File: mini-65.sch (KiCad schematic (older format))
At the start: 173 parts, among them J1 TYPE-C-31-M12_13_EDITED, J2 AVR-ISP-6, SW1 SW_Push, U1 ATmega32U4-AU, U2 WE-TVS-82400102, Y1 Crystal_GND24_Small

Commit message: changed layout of schematic
started the cleanup of the schematic, with nice lines and names above parts
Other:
- note added: "Mechanical Keyswitch Matrix"
- note added: "Microcontroller (atmega32u4)"
- moved on the sheet: C1, C2, C3, C4, C5, C6, C7, C8, D0, D1, D10, D11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

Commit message: Rearranged the schematic
Added lines and text to the different parts of the schematic
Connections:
- wire segments 313 -> 308
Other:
- note added: "Crystal"
- note added: "Decoupling Capacitors"
- note added: "ESD Protection TVS Diode"
- note added: "ICSP Header"
- note added: "Logos"
- note added: "Mounting Holes"
- note added: "Polyfuse"
- note added: "USB Type C"
- moved on the sheet: C1, C2, C3, C4, C5, C6, C7, C8, D0, D1, D10, D11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

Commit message: General schematic information added
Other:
- note added: "Electrical protection"
- note added: "mini eLiXiVy Schematic"
- moved on the sheet: C1, C2, C8, F1, H0, H1, H2, H3, H4, H5, J1, J2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

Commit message: Added different OSHW logo
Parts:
- removed D9: 1N4148W, mini-general-tweaks:D_SOD123_axial-dual, symbol Diode:1N4148W
- removed LO0: mini-eLiXiR-Logo-Mask, mini-Logos:eLiXiVy-Maskv2, symbol mini_random_library:mini-eLiXiR-Logo-Mask
- removed LO1: mini-eLiXiR-Logo-SilkScreen, mini-Logos:eLiXiVy-SilkScreenv2, symbol mini_random_library:mini-eLiXiR-Logo-SilkScreen
- added LO0: mini-eLiXiVy-SilkScreen, mini-Logos:eLiXiVy-SilkScreenv2, symbol mini_random_library:Logo
- added LO1: mini-eLiXiVy-Mask, mini-Logos:eLiXiVy-Maskv2, symbol mini_random_library:Logo
- added LO2: OSHW-Logo, mini-Logos:OSHW-Logo, symbol mini_random_library:Logo
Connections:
- wire segments 308 -> 307

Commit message: moved H3 mounting hole
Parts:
- added D9: 1N4148W, mini-general-tweaks:D_SOD123_axial-dual, symbol Diode:1N4148W
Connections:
- net ROW0: now also D9.1 (K)
- net at MX_9.2 (ROW): now also D9.2 (A)
- net DN: no longer names the net of R3.1, U1.3 (D-)
- net DP: no longer names the net of R2.1, U1.4 (D+)
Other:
- moved on the sheet: C1, C2, C3, C4, C5, C6, C7, C8, D0, D1, D10, D2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

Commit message: Shrunk schematic/matrix to fit on an A4 sheet
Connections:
- net ROW4: no longer D63.1 (K), D64.1 (K), D65.1 (K), D66.1 (K), D67.1 (K), D68.1 (K)
- new net: D63.1 (K), D64.1 (K), D65.1 (K), D66.1 (K), D67.1 (K), D68.1 (K)
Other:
- moved on the sheet: C1, C2, C3, C4, C5, C6, C7, C8, D10, F1, H0, H1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

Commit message: Rearranged the schematic to fit on an A4 sheet
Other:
- note added: "ESD TVS Diode"
- note added: "Electrical Protection"
- note removed: "ESD Protection TVS Diode"
- note removed: "Electrical protection"
- moved on the sheet: C1, C2, C3, C4, C5, C6, C7, C8, D0, D1, D10, D11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

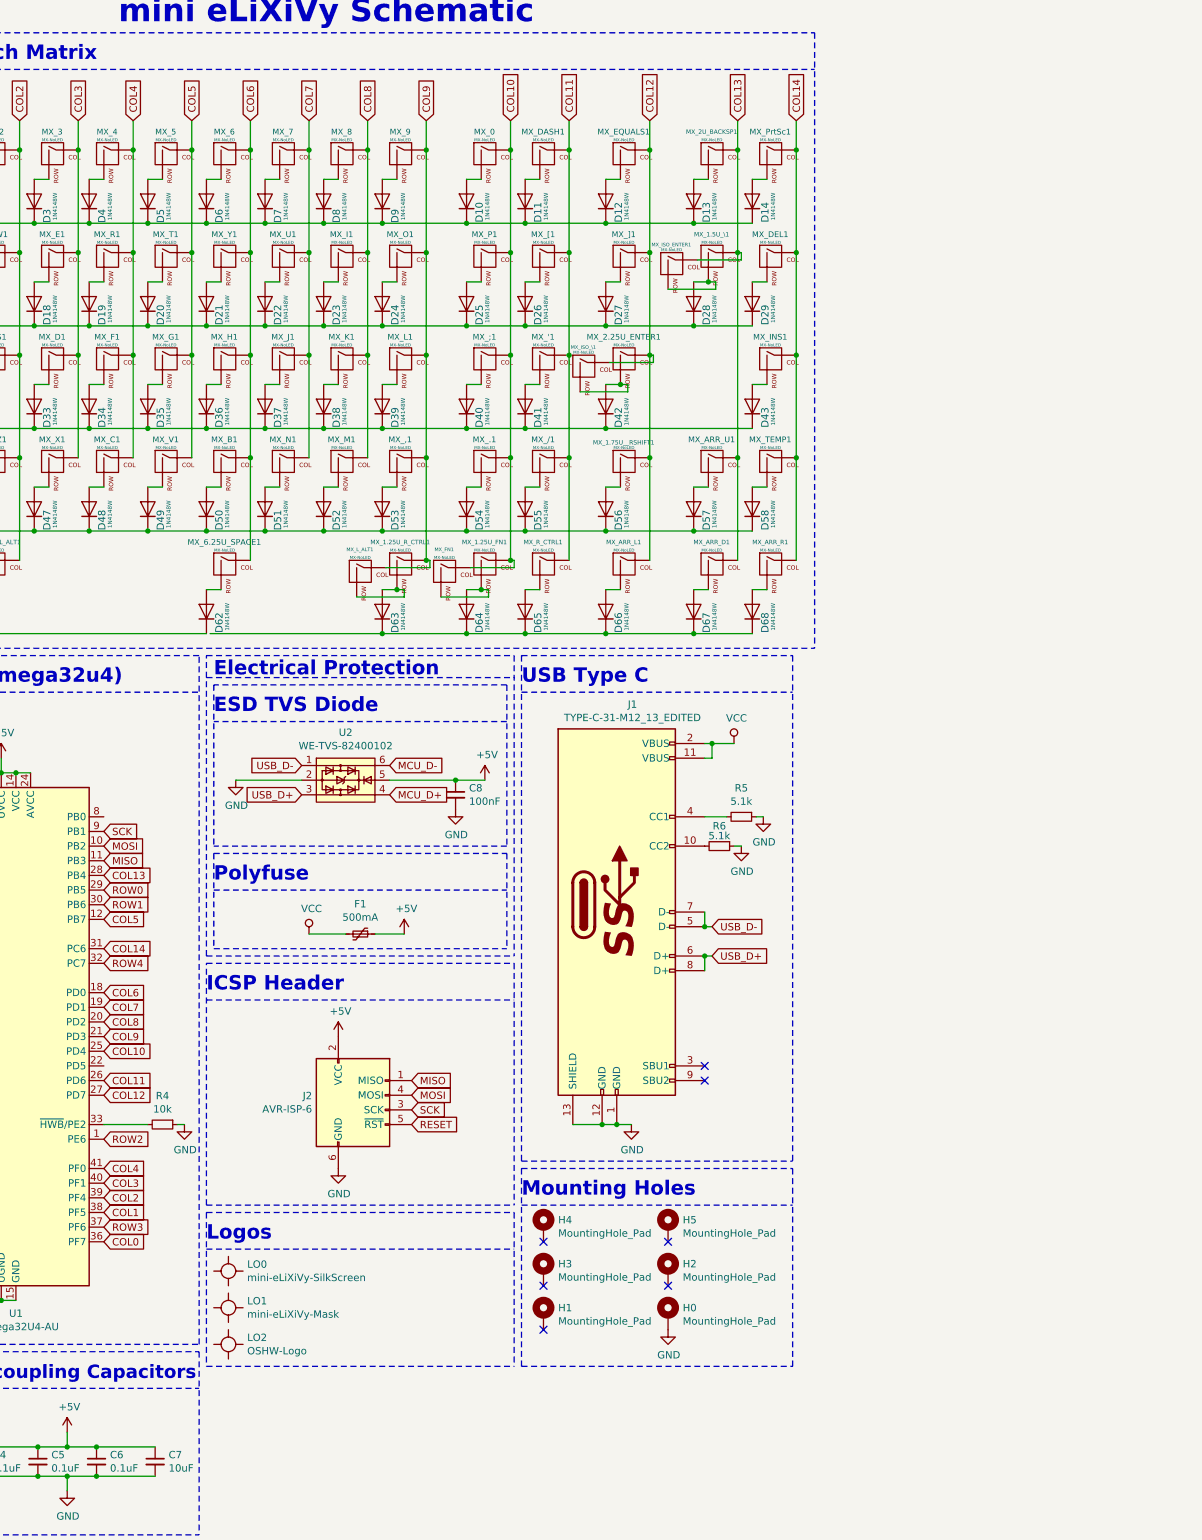
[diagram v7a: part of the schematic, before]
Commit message: Added rotary encoder first steps
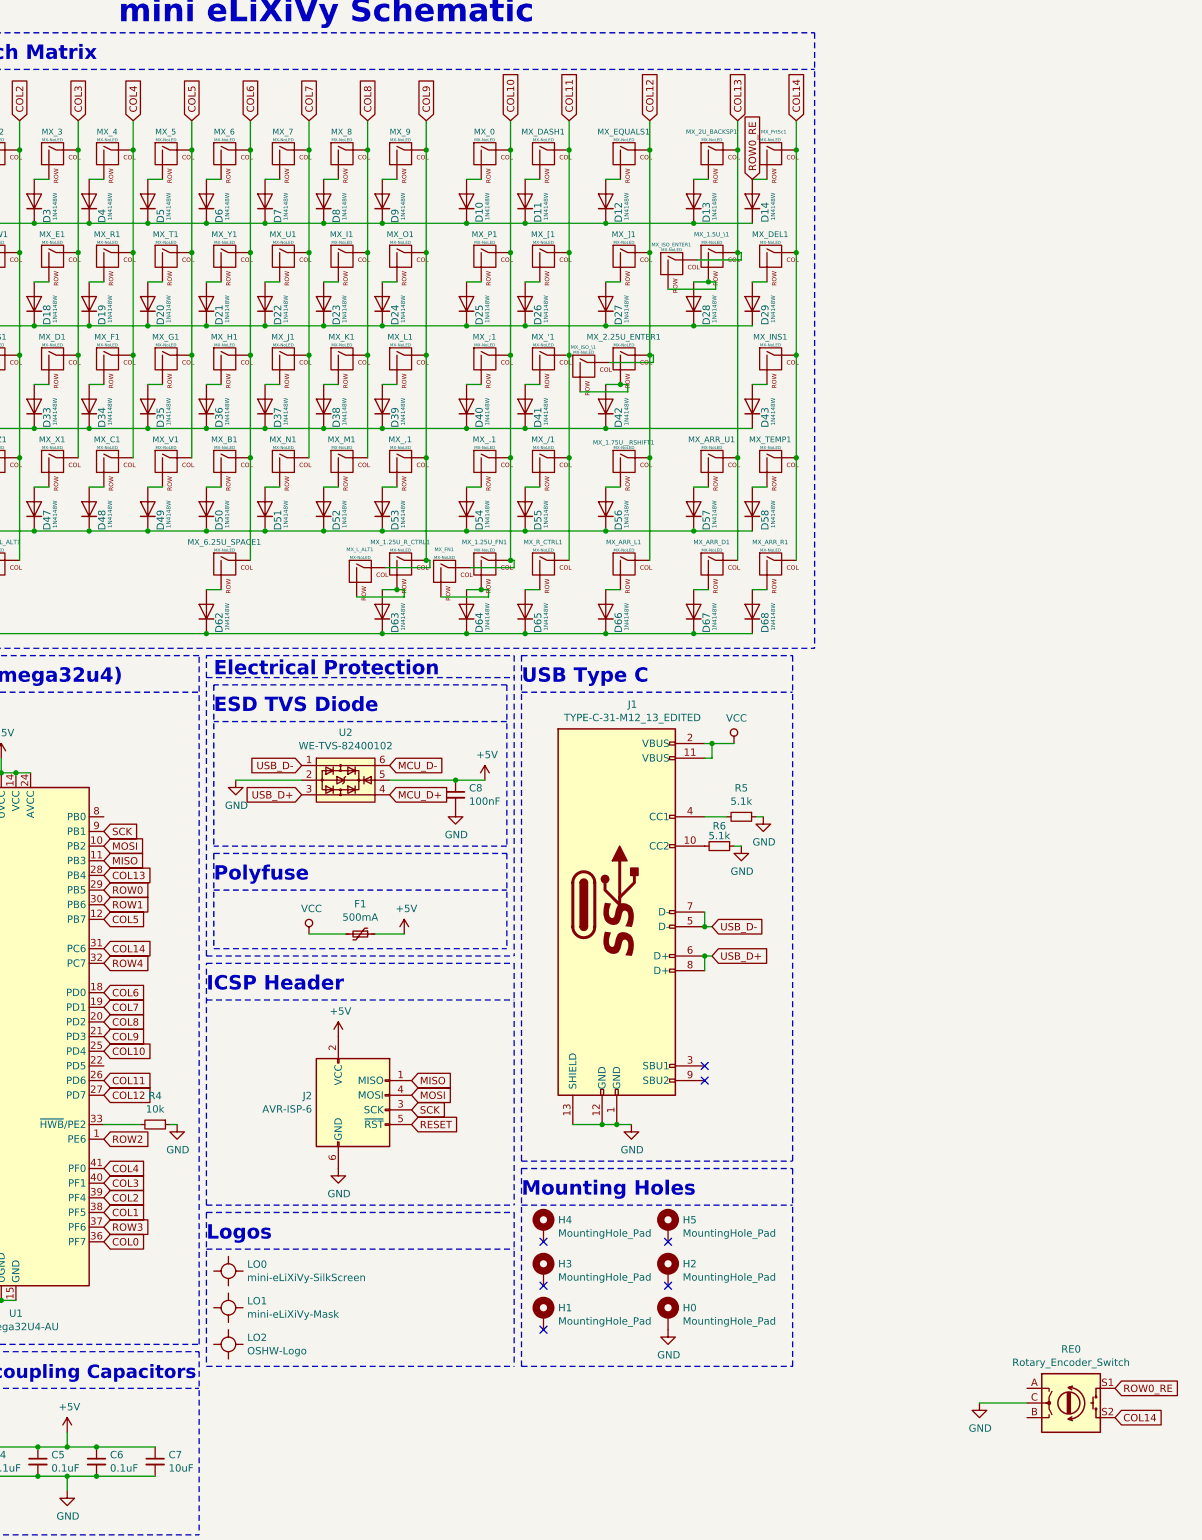
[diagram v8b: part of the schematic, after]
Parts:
- added RE0: Rotary_Encoder_Switch, Rotary_Encoder:RotaryEncoder_Alps_EC11E-Switch_Vertical_H20mm_CircularMountingHoles, symbol Device:Rotary_Encoder_Switch
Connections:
- net COL14: now also RE0.S2
- net GND: now also RE0.C
- net ROW4: now also D63.1 (K), D64.1 (K), D65.1 (K), D66.1 (K), D67.1 (K), D68.1 (K)
- net ROW0_RE: now reaches D14.2 (A), MX_PrtSc1.2 (ROW)
- net ROW0_RE: now also RE0.S1
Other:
- moved on the sheet: R4
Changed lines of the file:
@@
 Wire Wire Line
 	4750 4200 5325 4200
-Connection ~ 6275 4900
 Connection ~ 5725 4900
-Wire Wire Line
-	5725 4900 6275 4900
 Connection ~ 5325 4900
 Connection ~ 4750 4900
@@
 Wire Wire Line
 	3550 4200 3950 4200
-Wire Wire Line
-	6275 4900 6875 4900
 Wire Wire Line
 	6275 4200 6875 4200
@@
 Wire Wire Line
 	1975 4900 3550 4900
-Wire Wire Line
-	3575 4900 4750 4900
 Connection ~ 3850 3700
 Wire Wire Line
 	3850 3700 3850 4400
-Wire Wire Line
-	6875 4900 7275 4900
-Connection ~ 6875 4900
 Wire Wire Line
 	5325 4900 5725 4900
@@
 Wire Wire Line
 	900  2100 1100 2100
-Wire Wire Line
-	7175 3700 7175 4400
-Connection ~ 7175 3700
 Wire Wire Line
 	7175 2300 7175 3700
@@
 Wire Wire Line
 	7175 2300 7200 2300
-Wire Wire Line
-	6575 3700 6575 4400
-Connection ~ 6575 3700
 Wire Wire Line
 	6575 3000 6575 3700
@@
 $EndComp
 $Comp
-L Diode:1N4148W D68
-U 1 1 624EA389
-P 7275 4750
-F 0 "D68" H 7270 4663 50  0000 R CNN
-F 1 "1N4148W" H 7334 4608 28  0000 R CNN
-F 2 "mini-general-tweaks:D_SOD123_axial-dual" H 7275 4575 50  0001 C CNN
-F 3 "https://www.vishay.com/docs/85748/1n4148w.pdf" H 7275 4750 50  0001 C CNN
-	1    7275 4750
-	0    -1   -1   0
-$EndComp
-$Comp
-L Diode:1N4148W D67
-U 1 1 624DD549
-P 6875 4750
-F 0 "D67" H 6870 4663 50  0000 R CNN
-F 1 "1N4148W" H 6934 4608 28  0000 R CNN
-F 2 "mini-general-tweaks:D_SOD123_axial-dual" H 6875 4575 50  0001 C CNN
-F 3 "https://www.vishay.com/docs/85748/1n4148w.pdf" H 6875 4750 50  0001 C CNN
-	1    6875 4750
-	0    -1   -1   0
-$EndComp
-$Comp
-L Diode:1N4148W D66
-U 1 1 624D06BD
-P 6275 4750
-F 0 "D66" H 6270 4663 50  0000 R CNN
-F 1 "1N4148W" H 6334 4608 28  0000 R CNN
-F 2 "mini-general-tweaks:D_SOD123_axial-dual" H 6275 4575 50  0001 C CNN
-F 3 "https://www.vishay.com/docs/85748/1n4148w.pdf" H 6275 4750 50  0001 C CNN
-	1    6275 4750
-	0    -1   -1   0
-$EndComp
-$Comp
 L Diode:1N4148W D65
 U 1 1 624C36E1
@@
 	1250 3900 1250 3950
 Wire Wire Line
-	6975 4600 6875 4600
-$Comp
-L MX_Alps_Hybrid:MX-NoLED MX_ARR_D1
-U 1 1 5F474908
-P 7025 4450
-F 0 "MX_ARR_D1" H 6997 4624 30  0000 C CNN
-F 1 "MX-NoLED" H 6999 4569 20  0000 C CNN
-F 2 "mini-MX-Tweaks:MXOnly-1U-NoLED_tweak" H 6400 4425 60  0001 C CNN
-F 3 "" H 6400 4425 60  0001 C CNN
-	1    7025 4450
-	1    0    0    -1
-$EndComp
-Wire Wire Line
 	6975 2500 6875 2500
 $Comp
@@
 	7375 3900 7275 3900
 Wire Wire Line
-	7375 4600 7275 4600
-Wire Wire Line
 	7375 2500 7275 2500
 $Comp
@@
 $EndComp
 Connection ~ 6975 2500
-$Comp
-L MX_Alps_Hybrid:MX-NoLED MX_ARR_R1
-U 1 1 5F48B682
-P 7425 4450
-F 0 "MX_ARR_R1" H 7397 4624 30  0000 C CNN
-F 1 "MX-NoLED" H 7399 4569 20  0000 C CNN
-F 2 "mini-MX-Tweaks:MXOnly-1U-NoLED_tweak" H 6800 4425 60  0001 C CNN
-F 3 "" H 6800 4425 60  0001 C CNN
-	1    7425 4450
-	1    0    0    -1
-$EndComp
 Wire Wire Line
 	6975 3900 6875 3900
@@
 	6375 2500 6275 2500
 $Comp
-L MX_Alps_Hybrid:MX-NoLED MX_ARR_L1
-U 1 1 5F45D4BC
-P 6425 4450
-F 0 "MX_ARR_L1" H 6397 4624 30  0000 C CNN
-F 1 "MX-NoLED" H 6399 4569 20  0000 C CNN
-F 2 "mini-MX-Tweaks:MXOnly-1U-NoLED_tweak" H 5800 4425 60  0001 C CNN
-F 3 "" H 5800 4425 60  0001 C CNN
-	1    6425 4450
-	1    0    0    -1
-$EndComp
-Wire Wire Line
-	6375 4600 6275 4600
-$Comp
 L MX_Alps_Hybrid:MX-NoLED MX_1.75U_CAPSLOCK1
 U 1 1 5F1A606A
@@
 U 1 1 5F48B6A3
 P 7425 1650
-F 0 "MX_PrtSc1" H 7397 1824 39  0000 C CNN
+F 0 "MX_PrtSc1" H 7421 1824 24  0000 C CNN
 F 1 "MX-NoLED" H 7399 1769 20  0000 C CNN
 F 2 "mini-MX-Tweaks:MXOnly-1U-NoLED_tweak" H 6800 1625 60  0001 C CNN
@@
 L power:GND #PWR0104
 U 1 1 5F16F0E0
-P 3400 8250
-F 0 "#PWR0104" H 3400 8000 50  0001 C CNN
-F 1 "GND" H 3405 8077 50  0000 C CNN
-F 2 "" H 3400 8250 50  0001 C CNN
-F 3 "" H 3400 8250 50  0001 C CNN
-	1    3400 8250
-	1    0    0    -1
-$EndComp
-Wire Wire Line
-	3350 8250 3400 8250
+P 3350 8250
+F 0 "#PWR0104" H 3350 8000 50  0001 C CNN
+F 1 "GND" H 3355 8077 50  0000 C CNN
+F 2 "" H 3350 8250 50  0001 C CNN
+F 3 "" H 3350 8250 50  0001 C CNN
+	1    3350 8250
+	1    0    0    -1
+$EndComp
+Wire Wire Line
+	3300 8250 3350 8250
 $Comp
 L Device:R_Small R4
 U 1 1 5F16CB52
-P 3250 8250
-F 0 "R4" V 3054 8250 50  0000 C CNN
-F 1 "10k" V 3145 8250 50  0000 C CNN
-F 2 "Resistor_SMD:R_0805_2012Metric" H 3250 8250 50  0001 C CNN
-F 3 "~" H 3250 8250 50  0001 C CNN
-	1    3250 8250
+P 3200 8250
+F 0 "R4" V 3004 8250 50  0000 C CNN
+F 1 "10k" V 3095 8250 50  0000 C CNN
+F 2 "Resistor_SMD:R_0805_2012Metric" H 3200 8250 50  0001 C CNN
+F 3 "~" H 3200 8250 50  0001 C CNN
+	1    3200 8250
 	0    1    1    0
 $EndComp
-Wire Wire Line
-	2850 8250 3150 8250
 $Comp
 L power:GND #PWR0106
@@
 Wire Notes Line
 	1900 11050 3500 11050
+Wire Wire Line
+	3550 4900 4750 4900
+Connection ~ 3550 4900
+Text GLabel 7275 1800 1    50   Input ~ 0
+ROW0_RE
+Text GLabel 9750 10050 2    50   Input ~ 0
+ROW0_RE
+Text GLabel 9750 10250 2    50   Input ~ 0
+COL14
+$Comp
+L power:GND #PWR0123
+U 1 1 64F8DD45
+P 8825 10150
+F 0 "#PWR0123" H 8825 9900 50  0001 C CNN
+F 1 "GND" H 8830 9977 50  0000 C CNN
+F 2 "" H 8825 10150 50  0001 C CNN
+F 3 "" H 8825 10150 50  0001 C CNN
+	1    8825 10150
+	1    0    0    -1
+$EndComp
+Wire Wire Line
+	8825 10150 9150 10150
+$Comp
+L Device:Rotary_Encoder_Switch RE0
+U 1 1 64FB0777
+P 9450 10150
+F 0 "RE0" H 9450 10517 50  0000 C CNN
+F 1 "Rotary_Encoder_Switch" H 9450 10426 50  0000 C CNN
+F 2 "Rotary_Encoder:RotaryEncoder_Alps_EC11E-Switch_Vertical_H20mm_CircularMountingHoles" H 9300 10310 50  0001 C CNN
+F 3 "~" H 9450 10410 50  0001 C CNN
+	1    9450 10150
+	1    0    0    -1
+$EndComp
+Wire Wire Line
+	2850 8250 3100 8250
+Connection ~ 6575 3700
+Connection ~ 7175 3700
+Connection ~ 6875 4900
+Wire Wire Line
+	6875 4900 7275 4900
+Wire Wire Line
+	6275 4900 6875 4900
+Wire Wire Line
+	5725 4900 6275 4900
+Connection ~ 6275 4900
+Wire Wire Line
+	6375 4600 6275 4600
+$Comp
+L MX_Alps_Hybrid:MX-NoLED MX_ARR_L1
+U 1 1 5F45D4BC
+P 6425 4450
+F 0 "MX_ARR_L1" H 6397 4624 30  0000 C CNN
+F 1 "MX-NoLED" H 6399 4569 20  0000 C CNN
+F 2 "mini-MX-Tweaks:MXOnly-1U-NoLED_tweak" H 5800 4425 60  0001 C CNN
+F 3 "" H 5800 4425 60  0001 C CNN
+	1    6425 4450
+	1    0    0    -1
+$EndComp
+$Comp
+L MX_Alps_Hybrid:MX-NoLED MX_ARR_R1
+U 1 1 5F48B682
+P 7425 4450
+F 0 "MX_ARR_R1" H 7397 4624 30  0000 C CNN
+F 1 "MX-NoLED" H 7399 4569 20  0000 C CNN
+F 2 "mini-MX-Tweaks:MXOnly-1U-NoLED_tweak" H 6800 4425 60  0001 C CNN
+F 3 "" H 6800 4425 60  0001 C CNN
+	1    7425 4450
+	1    0    0    -1
+$EndComp
+Wire Wire Line
+	7375 4600 7275 4600
+$Comp
+L MX_Alps_Hybrid:MX-NoLED MX_ARR_D1
+U 1 1 5F474908
+P 7025 4450
+F 0 "MX_ARR_D1" H 6997 4624 30  0000 C CNN
+F 1 "MX-NoLED" H 6999 4569 20  0000 C CNN
+F 2 "mini-MX-Tweaks:MXOnly-1U-NoLED_tweak" H 6400 4425 60  0001 C CNN
+F 3 "" H 6400 4425 60  0001 C CNN
+	1    7025 4450
+	1    0    0    -1
+$EndComp
+Wire Wire Line
+	6975 4600 6875 4600
+$Comp
+L Diode:1N4148W D66
+U 1 1 624D06BD
+P 6275 4750
+F 0 "D66" H 6270 4663 50  0000 R CNN
+F 1 "1N4148W" H 6334 4608 28  0000 R CNN
+F 2 "mini-general-tweaks:D_SOD123_axial-dual" H 6275 4575 50  0001 C CNN
+F 3 "https://www.vishay.com/docs/85748/1n4148w.pdf" H 6275 4750 50  0001 C CNN
+	1    6275 4750
+	0    -1   -1   0
+$EndComp
+$Comp
+L Diode:1N4148W D67
+U 1 1 624DD549
+P 6875 4750
+F 0 "D67" H 6870 4663 50  0000 R CNN
+F 1 "1N4148W" H 6934 4608 28  0000 R CNN
+F 2 "mini-general-tweaks:D_SOD123_axial-dual" H 6875 4575 50  0001 C CNN
+F 3 "https://www.vishay.com/docs/85748/1n4148w.pdf" H 6875 4750 50  0001 C CNN
+	1    6875 4750
+	0    -1   -1   0
+$EndComp
+$Comp
+L Diode:1N4148W D68
+U 1 1 624EA389
+P 7275 4750
+F 0 "D68" H 7270 4663 50  0000 R CNN
+F 1 "1N4148W" H 7334 4608 28  0000 R CNN
+F 2 "mini-general-tweaks:D_SOD123_axial-dual" H 7275 4575 50  0001 C CNN
+F 3 "https://www.vishay.com/docs/85748/1n4148w.pdf" H 7275 4750 50  0001 C CNN
+	1    7275 4750
+	0    -1   -1   0
+$EndComp
+Wire Wire Line
+	6575 3700 6575 4400
+Wire Wire Line
+	7175 3700 7175 4400
 $EndSCHEMATC
